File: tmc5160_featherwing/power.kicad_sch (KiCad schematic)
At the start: 10 parts, among them J1 Conn_01x03_P2.54MM_HeaderHoles, J2 Conn_01x02_P1.5MM_Molex_Pico-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, J3 Conn_01x03_P2.54MM_HeaderHoles, U1 3.3V_100MA

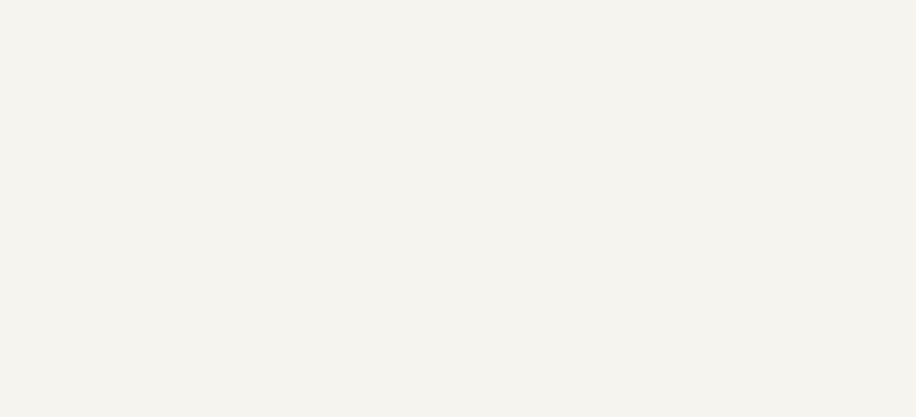
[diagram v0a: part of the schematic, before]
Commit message: Add fan
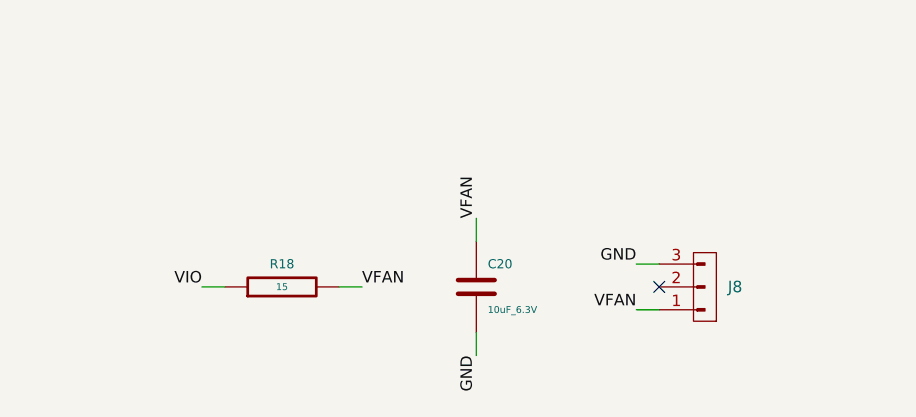
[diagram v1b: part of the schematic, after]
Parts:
- added C20: 10uF_6.3V, Janelia:C_0402_1005Metric, symbol Janelia:C_10uF_6.3V_0402
- added J8: HEADER_01X03_JST_SUR_VERTICAL, Janelia:JST_SUR_BM03B-SURS-TF_1x03-1MP_P0.80mm_Vertical, symbol Janelia:HEADER_01X03_JST_SUR_VERTICAL
- added R18: 15, Janelia:R_0402_1005Metric, symbol Janelia:R_15_0.1W_0402
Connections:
- net GND: now also C20.2, J8.3 (Pin_3)
- net VIO: now also R18.1
- new net VFAN: C20.1, J8.1 (Pin_1), R18.2
- no-connect marks 2 -> 3
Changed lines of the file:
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@@
   (title_block
     (title "tmc5160_featherwing")
-    (date "2024-04-12")
+    (date "2024-04-15")
     (rev "1.0")
     (company "Howard Hughes Medical Institute")
@@
   (no_connect (at 179.07 99.06))
   (no_connect (at 179.07 101.6))
+  (no_connect (at 115.57 166.37))
+  (wire (pts (xy 115.57 168.91) (xy 113.03 168.91))
+    (stroke (width 0) (type default))
+  )
   (wire (pts (xy 148.59 101.6) (xy 146.05 101.6))
     (stroke (width 0) (type default))
@@
     (stroke (width 0) (type default))
   )
+  (wire (pts (xy 95.25 171.45) (xy 95.25 173.99))
+    (stroke (width 0) (type default))
+  )
+  (wire (pts (xy 115.57 163.83) (xy 113.03 163.83))
+    (stroke (width 0) (type default))
+  )
   (wire (pts (xy 179.07 96.52) (xy 181.61 96.52))
     (stroke (width 0) (type default))
@@
     (stroke (width 0) (type default))
   )
+  (wire (pts (xy 80.01 166.37) (xy 82.55 166.37))
+    (stroke (width 0) (type default))
+  )
   (wire (pts (xy 100.33 102.87) (xy 100.33 105.41))
     (stroke (width 0) (type default))
@@
     (stroke (width 0) (type default))
   )
+  (wire (pts (xy 67.31 166.37) (xy 64.77 166.37))
+    (stroke (width 0) (type default))
+  )
   (wire (pts (xy 148.59 96.52) (xy 146.05 96.52))
     (stroke (width 0) (type default))
   )
+  (wire (pts (xy 95.25 161.29) (xy 95.25 158.75))
+    (stroke (width 0) (type default))
+  )
   (label "GND" (at 100.33 105.41 270) (fields_autoplaced)
     (effects (font (size 1.27 1.27)) (justify right bottom))
   )
+  (label "GND" (at 113.03 163.83 180) (fields_autoplaced)
+    (effects (font (size 1.27 1.27)) (justify right bottom))
+  )
   (label "VM" (at 100.33 77.47 90) (fields_autoplaced)
     (effects (font (size 1.27 1.27)) (justify left bottom))
@@
     (effects (font (size 1.27 1.27)) (justify right bottom))
   )
+  (label "VFAN" (at 95.25 158.75 90) (fields_autoplaced)
+    (effects (font (size 1.27 1.27)) (justify left bottom))
+  )
+  (label "VIO" (at 64.77 166.37 180) (fields_autoplaced)
+    (effects (font (size 1.27 1.27)) (justify right bottom))
+  )
   (label "GND" (at 124.46 106.68 270) (fields_autoplaced)
     (effects (font (size 1.27 1.27)) (justify right bottom))
@@
     (effects (font (size 1.27 1.27)) (justify right bottom))
   )
+  (label "GND" (at 95.25 173.99 270) (fields_autoplaced)
+    (effects (font (size 1.27 1.27)) (justify right bottom))
+  )
+  (label "VFAN" (at 113.03 168.91 180) (fields_autoplaced)
+    (effects (font (size 1.27 1.27)) (justify right bottom))
+  )
   (label "GND" (at 208.28 105.41 270) (fields_autoplaced)
     (effects (font (size 1.27 1.27)) (justify right bottom))
@@
   )
   (label "ENABLE" (at 55.88 102.87 0) (fields_autoplaced)
+    (effects (font (size 1.27 1.27)) (justify left bottom))
+  )
+  (label "VFAN" (at 82.55 166.37 0) (fields_autoplaced)
     (effects (font (size 1.27 1.27)) (justify left bottom))
   )
@@
   (hierarchical_label "ENABLE" (shape input) (at 53.34 102.87 180) (fields_autoplaced)
     (effects (font (size 1.27 1.27)) (justify right))
+  )
+  (symbol (lib_id "Janelia:HEADER_01X03_JST_SUR_VERTICAL") (at 120.65 166.37 180) (unit 1)
+    (in_bom yes) (on_board yes) (dnp no) (fields_autoplaced)
+    (property "Reference" "J8" (at 123.19 166.37 0)
+      (effects (font (size 1.27 1.27)) (justify right))
+    )
+    (property "Value" "HEADER_01X03_JST_SUR_VERTICAL" (at 120.65 161.29 0)
+      (effects (font (size 1.27 1.27)) hide)
+    )
+    (property "Footprint" "Janelia:JST_SUR_BM03B-SURS-TF_1x03-1MP_P0.80mm_Vertical" (at 120.65 179.07 0)
+      (effects (font (size 1.27 1.27)) hide)
+    )
+    (property "Datasheet" "" (at 120.65 166.37 0)
+      (effects (font (size 1.27 1.27)) hide)
+    )
+    (property "Description" "CONN HEADER SMD 3POS 0.8MM" (at 120.65 176.53 0)
+      (effects (font (size 1.27 1.27)) hide)
+    )
+    (property "Manufacturer" "JST Sales America Inc." (at 120.65 184.15 0)
+      (effects (font (size 1.27 1.27)) hide)
+    )
+    (property "Manufacturer Part Number" "BM03B-SURS-TF" (at 120.65 181.61 0)
+      (effects (font (size 1.27 1.27)) hide)
+    )
+    (property "Vendor" "Digi-Key" (at 120.65 186.69 0)
+      (effects (font (size 1.27 1.27)) hide)
+    )
+    (property "Vendor Part Number" "455-3586-1-ND" (at 120.65 189.23 0)
+      (effects (font (size 1.27 1.27)) hide)
+    )
+    (property "Sim.Enable" "0" (at 120.65 166.37 0)
+      (effects (font (size 1.27 1.27)) hide)
+    )
+    (pin "2")
+    (pin "1")
+    (pin "3")
+    (instances
+      (project "tmc5160_featherwing"
+        (path "/df2b2e89-e055-4140-95de-f1df723db034/c1dd8f61-494c-402f-8e59-08309c64fc3f"
+          (reference "J8") (unit 1)
+        )
+      )
+    )
+  )
+  (symbol (lib_id "Janelia:C_10uF_6.3V_0402") (at 95.25 166.37 0) (unit 1)
+    (in_bom yes) (on_board yes) (dnp no)
+    (property "Reference" "C20" (at 96.52 163.83 0)
+      (effects (font (size 1.016 1.016)) (justify left))
+    )
+    (property "Value" "10uF_6.3V" (at 96.52 168.91 0)
+      (effects (font (size 0.762 0.762)) (justify left))
+    )
+    (property "Footprint" "Janelia:C_0402_1005Metric" (at 96.2152 170.18 0)
+      (effects (font (size 0.762 0.762)) hide)
+    )
+    (property "Datasheet" "" (at 95.25 166.37 0)
+      (effects (font (size 1.524 1.524)))
+    )
+    (property "Vendor" "Digi-Key" (at 97.79 161.29 0)
+      (effects (font (size 1.524 1.524)) hide)
+    )
+    (property "Vendor Part Number" "490-GRT155R60J106ME13JCT-ND" (at 100.33 158.75 0)
+      (effects (font (size 1.524 1.524)) hide)
+    )
+    (property "Description" "CAP CER 10UF 6.3V X5R" (at 102.87 156.21 0)
+      (effects (font (size 1.524 1.524)) hide)
+    )
+    (property "Package" "0402" (at 95.25 166.37 0)
+      (effects (font (size 1.27 1.27)) hide)
+    )
+    (property "Manufacturer" "Murata Electronics" (at 95.25 166.37 0)
+      (effects (font (size 1.27 1.27)) hide)
+    )
+    (property "Manufacturer Part Number" "GRT155R60J106ME13J" (at 95.25 166.37 0)
+      (effects (font (size 1.27 1.27)) hide)
+    )
+    (pin "2")
+    (pin "1")
+    (instances
+      (project "tmc5160_featherwing"
+        (path "/df2b2e89-e055-4140-95de-f1df723db034/c1dd8f61-494c-402f-8e59-08309c64fc3f"
+          (reference "C20") (unit 1)
+        )
+      )
+    )
   )
   (symbol (lib_id "Janelia:Conn_01x03_P2.54MM_HeaderHoles") (at 83.82 107.95 0) (unit 1)
@@
         )
       )
+    )
+  )
+  (symbol (lib_id "Janelia:R_15_0.1W_0402") (at 73.66 166.37 90) (unit 1)
+    (in_bom yes) (on_board yes) (dnp no)
+    (property "Reference" "R18" (at 73.66 163.83 90)
+      (effects (font (size 1.016 1.016)))
+    )
+    (property "Value" "15" (at 73.66 166.37 90) (do_not_autoplace)
+      (effects (font (size 0.762 0.762)))
+    )
+    (property "Footprint" "Janelia:R_0402_1005Metric" (at 73.66 168.148 90)
+      (effects (font (size 0.762 0.762)) hide)
+    )
+    (property "Datasheet" "" (at 73.66 164.338 90)
+      (effects (font (size 0.762 0.762)))
+    )
+    (property "Vendor" "Digi-Key" (at 71.12 161.798 90)
+      (effects (font (size 1.524 1.524)) hide)
+    )
+    (property "Vendor Part Number" "P15.0LCT-ND" (at 68.58 159.258 90)
+      (effects (font (size 1.524 1.524)) hide)
+    )
+    (property "Description" "RES SMD 15 OHM 1% 1/10W" (at 66.04 156.718 90)
+      (effects (font (size 1.524 1.524)) hide)
+    )
+    (property "Package" "0402" (at 73.66 166.37 0)
+      (effects (font (size 1.27 1.27)) hide)
+    )
+    (property "Manufacturer" "Panasonic Electronic Components" (at 73.66 166.37 0)
+      (effects (font (size 1.27 1.27)) hide)
+    )
+    (property "Manufacturer Part Number" "ERJ-2RKF15R0X" (at 73.66 166.37 0)
+      (effects (font (size 1.27 1.27)) hide)
+    )
+    (pin "2")
+    (pin "1")
+    (instances
+      (project "tmc5160_featherwing"
+        (path "/df2b2e89-e055-4140-95de-f1df723db034/c1dd8f61-494c-402f-8e59-08309c64fc3f"
+          (reference "R18") (unit 1)
+        )
+      )

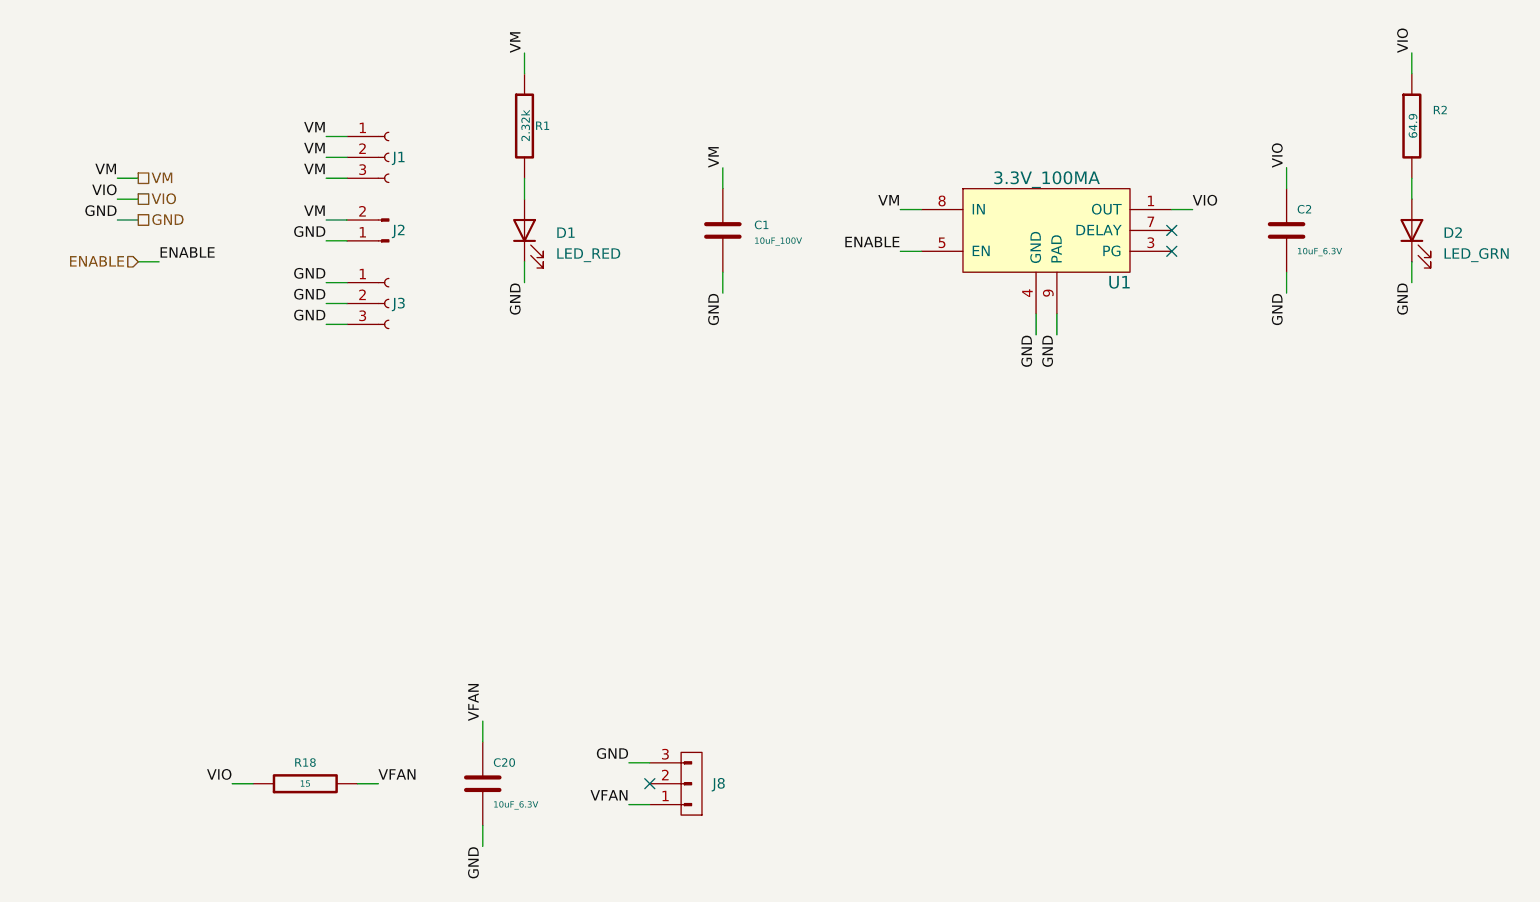
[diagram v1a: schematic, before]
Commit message: Add enable_fan
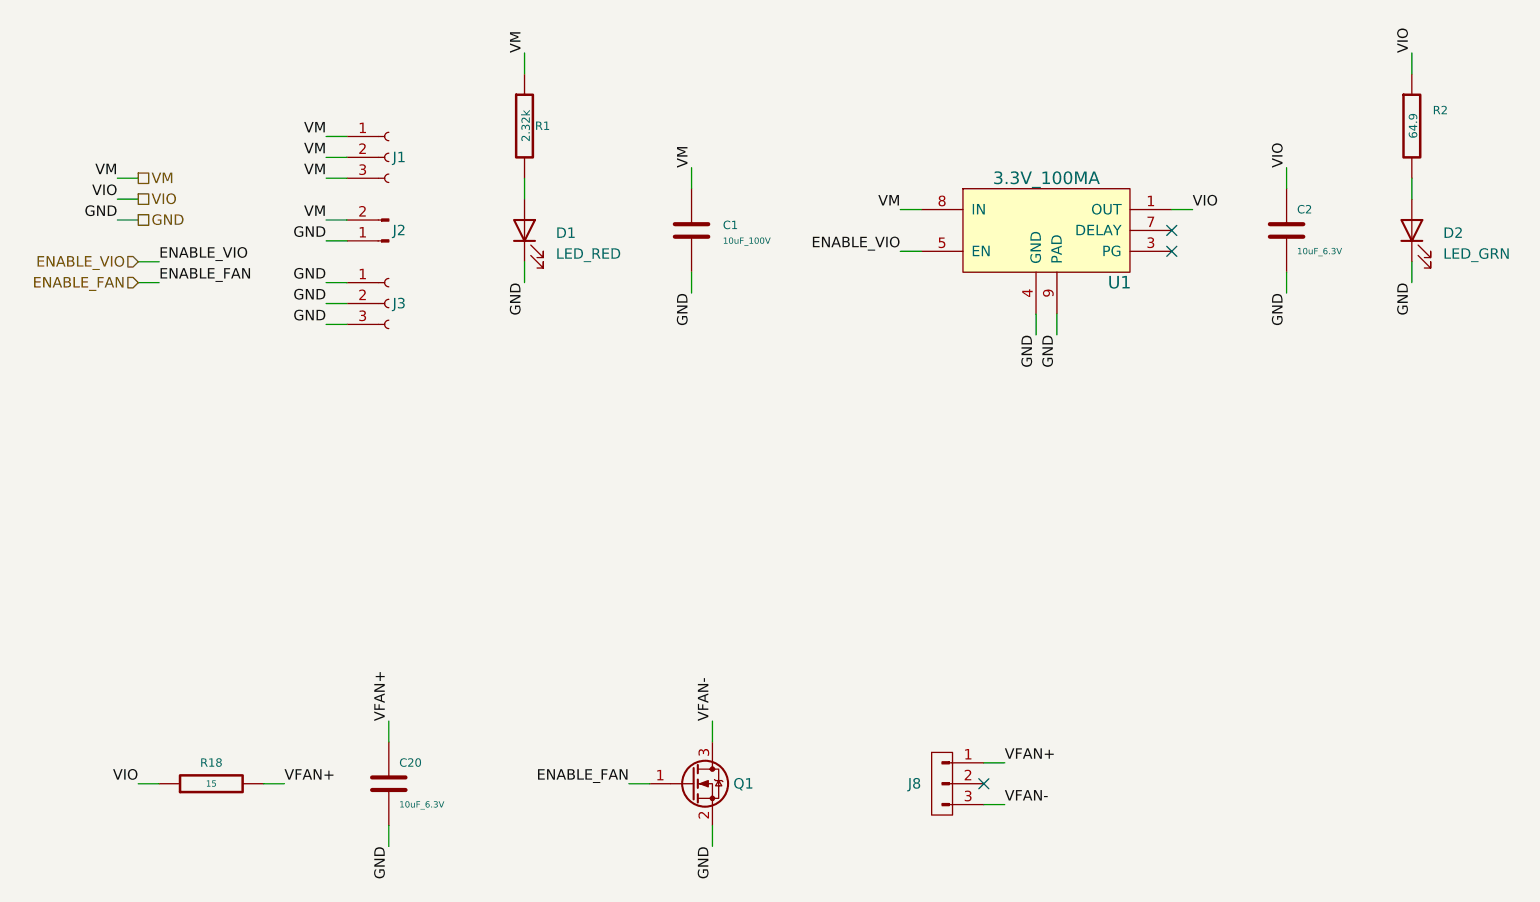
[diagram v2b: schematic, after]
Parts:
- added Q1: MOSFET-N-CH, Janelia:XFDFN-3, symbol Janelia:MOSFET-N-CH-EN-CSD17483F4
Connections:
- net GND: now also Q1.2 (S); no longer J8.3 (Pin_3)
- net ENABLE renamed ENABLE_VIO
- net VFAN renamed VFAN+
- new net ENABLE_FAN: Q1.1 (G)
- new net VFAN-: J8.3 (Pin_3), Q1.3 (D)
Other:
- moved on the sheet: C1, C20, J8, R18
